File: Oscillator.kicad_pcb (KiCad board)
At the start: 2 copper layers, 200.9 x 113.3 mm, 231 parts, among them J201 AudioJack2, J202 AudioJack2, J203 AudioJack2, J204 Conn_01x14, J205 AudioJack2, J206 AudioJack2, J207 Conn_01x09, J208 AudioJack2, J209 AudioJack2, J210 AudioJack2, J301 Conn_01x14, J302 Conn_01x09, J303 Conn_02x05_Odd_Even, Q401 2N3904, Q402 2N3906, Q403 2N3904, Q601 Q_NJFET_DSG, Q602 Q_NJFET_DSG, Q603 2N3904, Q701 Q_NJFET_DSG, SW201 SR1712F-0204-20F0A-N9-N-027, U201 TL072, U402 LM13700, U501 TL074, U502 LM13700, U503 TL074, U601 TL074, U602 LM339, U603 TL074, U604 4066, U605 TL074, U701 OP275, U702 DMMT3904W, U703 TL072

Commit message: Added version markings
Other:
- board text added: "oscillator / waveshaper / vca version 2 chris defrancisci"
- board text removed: "oscillator / waveshaper / vca version 1 chris defrancisci"

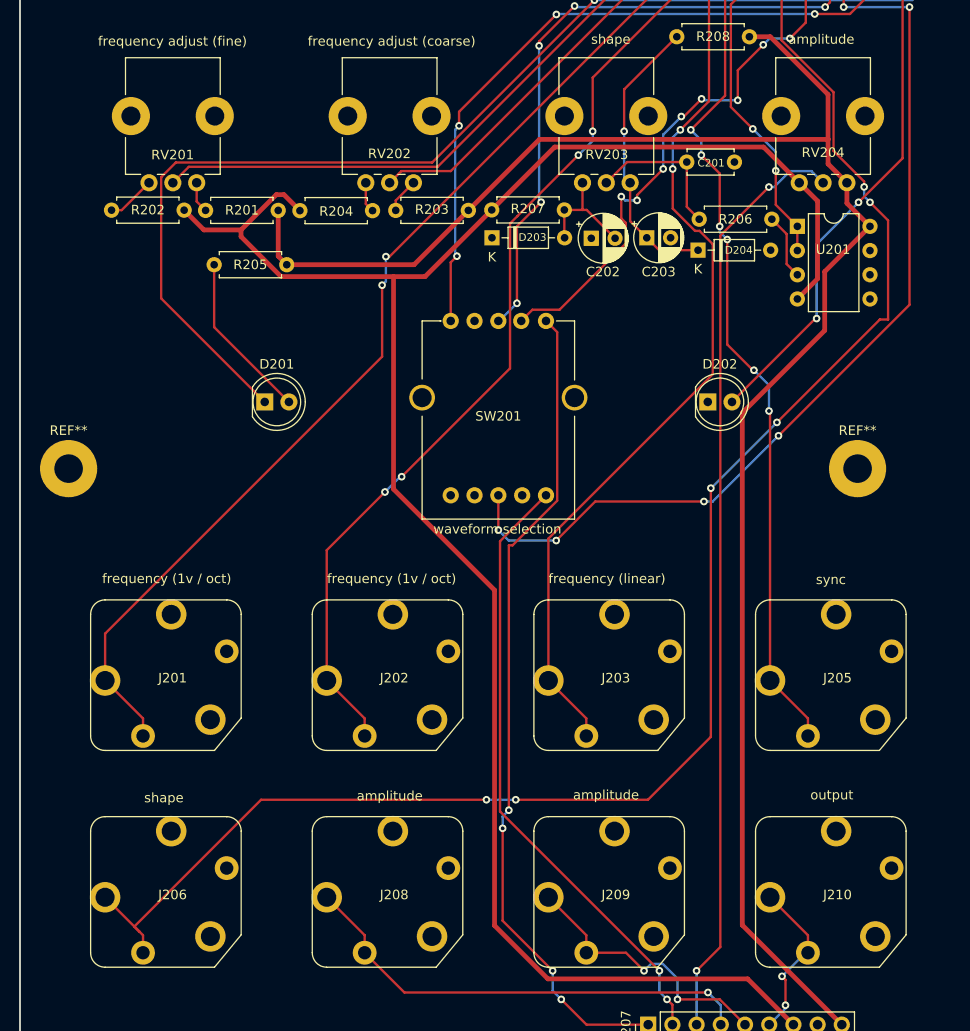
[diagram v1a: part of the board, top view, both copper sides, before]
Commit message: Updated for tayda pots A-5513 and jacks A-2563
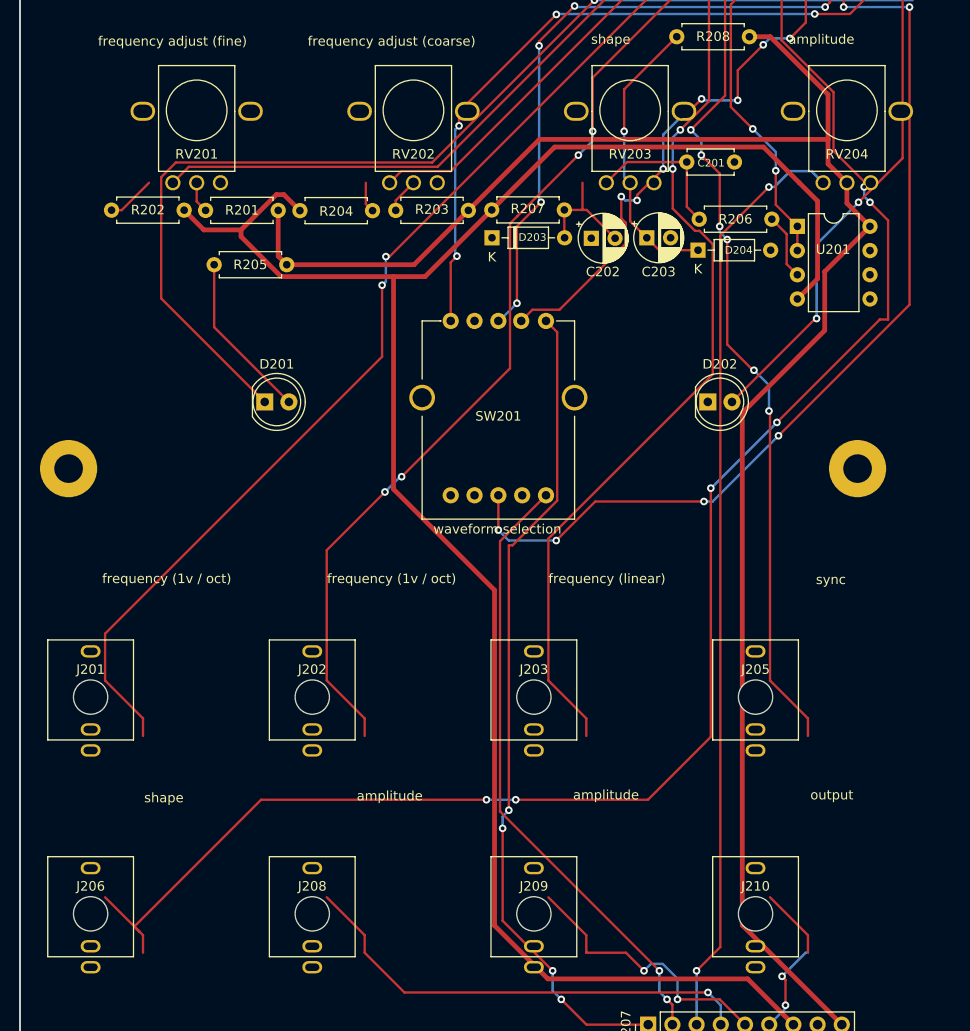
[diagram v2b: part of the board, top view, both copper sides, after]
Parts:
- J201, J202, J203, J205, J206, J208, J209, J210: footprint ACJM-MV35:ACJM-MV35 -> A-2563:A-2563
- RV201, RV202, RV203, RV204: footprint Potentiometer_THT:Potentiometer_Bourns_PTV09A-1_Single_Vertical -> A-5513:A-5513
- turned RV201 to 0 degrees
- turned RV202 to 0 degrees
- turned RV203 to 0 degrees
- turned RV204 to 0 degrees
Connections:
- RV201 pad 1: Net-(R201-Pad2) -> Net-(R202-Pad1)
- RV201 pad 3: Net-(R202-Pad1) -> Net-(R201-Pad2)
- RV202 pad 1: Net-(R203-Pad2) -> Net-(R204-Pad1)
- RV202 pad 3: Net-(R204-Pad1) -> Net-(R203-Pad2)
- RV203 pad 1: Net-(C203-Pad1) -> Net-(C202-Pad2)
- RV203 pad 3: Net-(C202-Pad2) -> Net-(C203-Pad1)
- RV204 pad 1: +12V -> -12V
- RV204 pad 3: -12V -> +12V

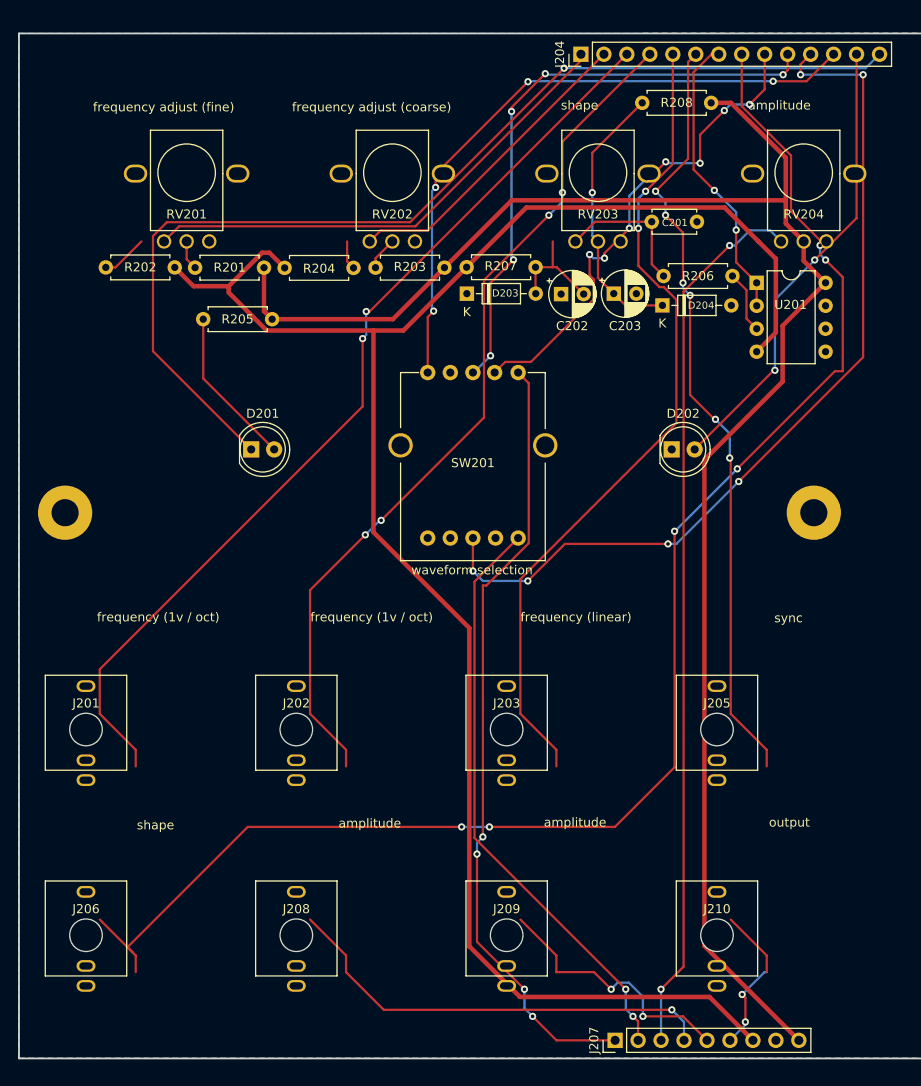
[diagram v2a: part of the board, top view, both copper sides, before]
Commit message: Arranging/connecting new knobs/jacks
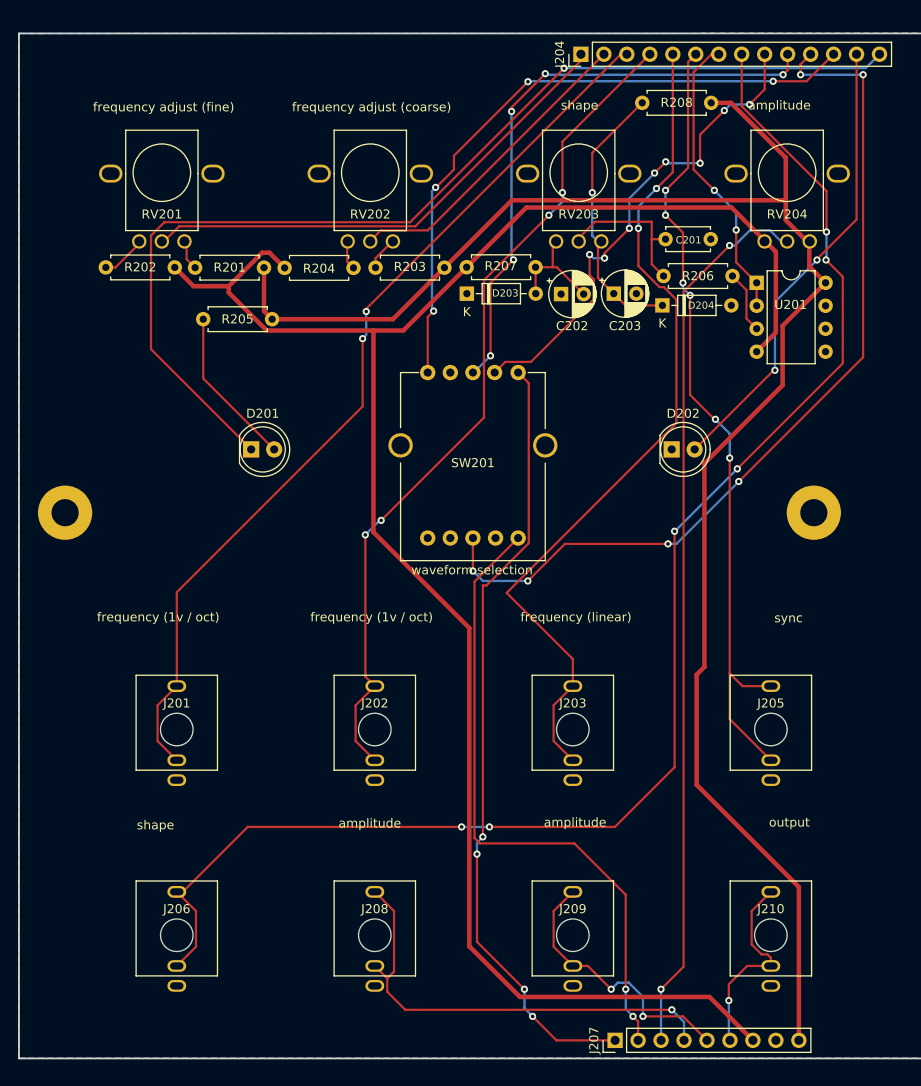
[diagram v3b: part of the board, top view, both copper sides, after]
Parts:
- moved J201 10.0 mm to (84.5, 112.6)
- moved J206 10.0 mm to (84.5, 135.3)
- moved J202 8.68 mm to (106.4, 112.6)
- moved J208 8.68 mm to (106.4, 135.3)
- moved J203 7.32 mm to (128.3, 112.6)
- moved J209 7.32 mm to (128.3, 135.3)
- moved J205 5.96 mm to (150.2, 112.6)
- moved J210 5.96 mm to (150.2, 135.3)
- moved RV201 2.74 mm to (82.8, 53.0)
- moved C201 2.46 mm to (138.6, 52.8)
- moved RV202 2.44 mm to (105.9, 53.0)
- moved RV203 2.13 mm to (128.9, 53.0)
- moved RV204 1.83 mm to (152.0, 53.0)
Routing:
- net /panel/shape_cv: track 168.7 -> 162.0 mm
- net /panel/waveshaper_bypass: track 65.0 -> 71.2 mm
- net /panel/out: track 17.1 -> 22.1 mm, vias 2 -> 1
- net /panel/fm_cv1: track 104.8 -> 100.8 mm
- net /panel/sync: track 85.7 -> 89.6 mm
- net /panel/fm_cv_lin: track 91.1 -> 94.2 mm
- net /panel/fm_cv2: track 96.1 -> 93.4 mm
- net Net-(C201-Pad1): track 15.9 -> 17.4 mm
- net /panel/vca_cv1: track 49.2 -> 50.4 mm
- net /panel/vca_cv2: track 29.1 -> 30.1 mm
- net +12V: track 687.9 -> 688.6 mm

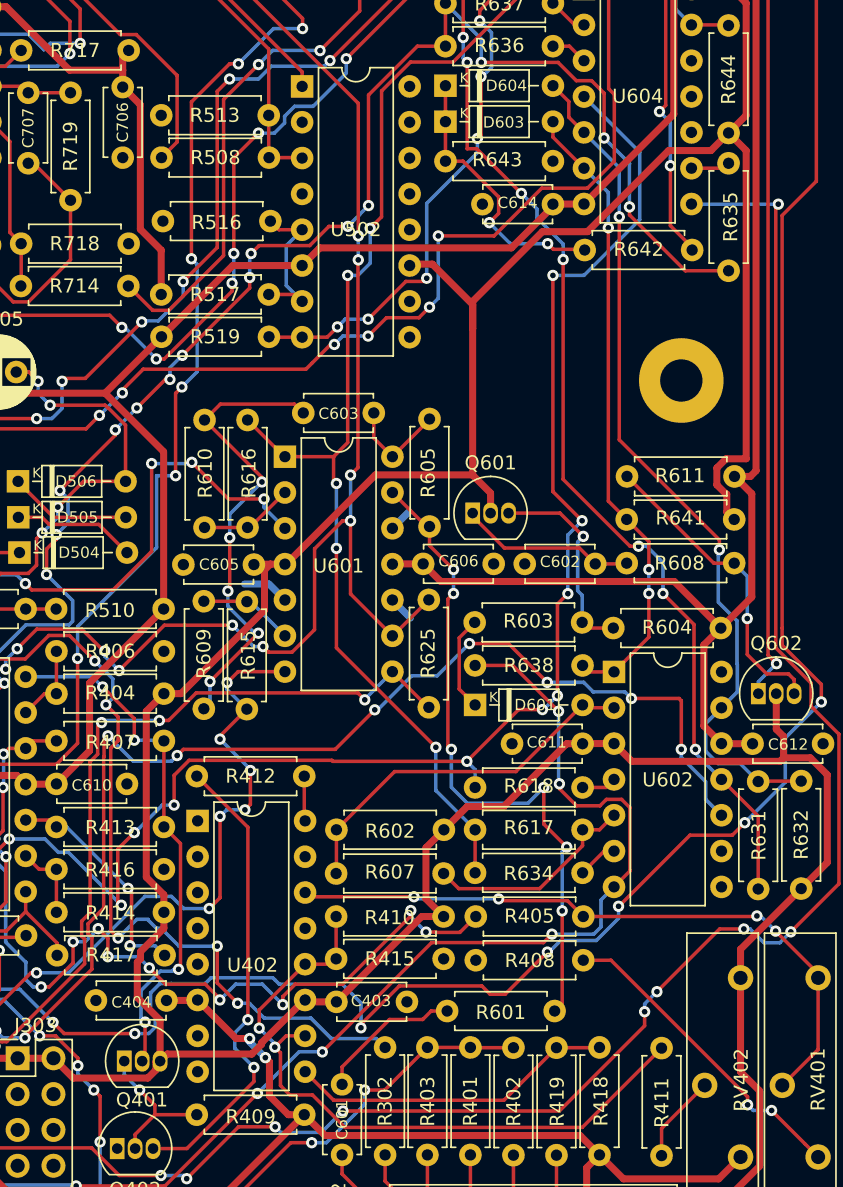
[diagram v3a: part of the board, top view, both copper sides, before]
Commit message: Routed consolidate lm13700, ran DRC
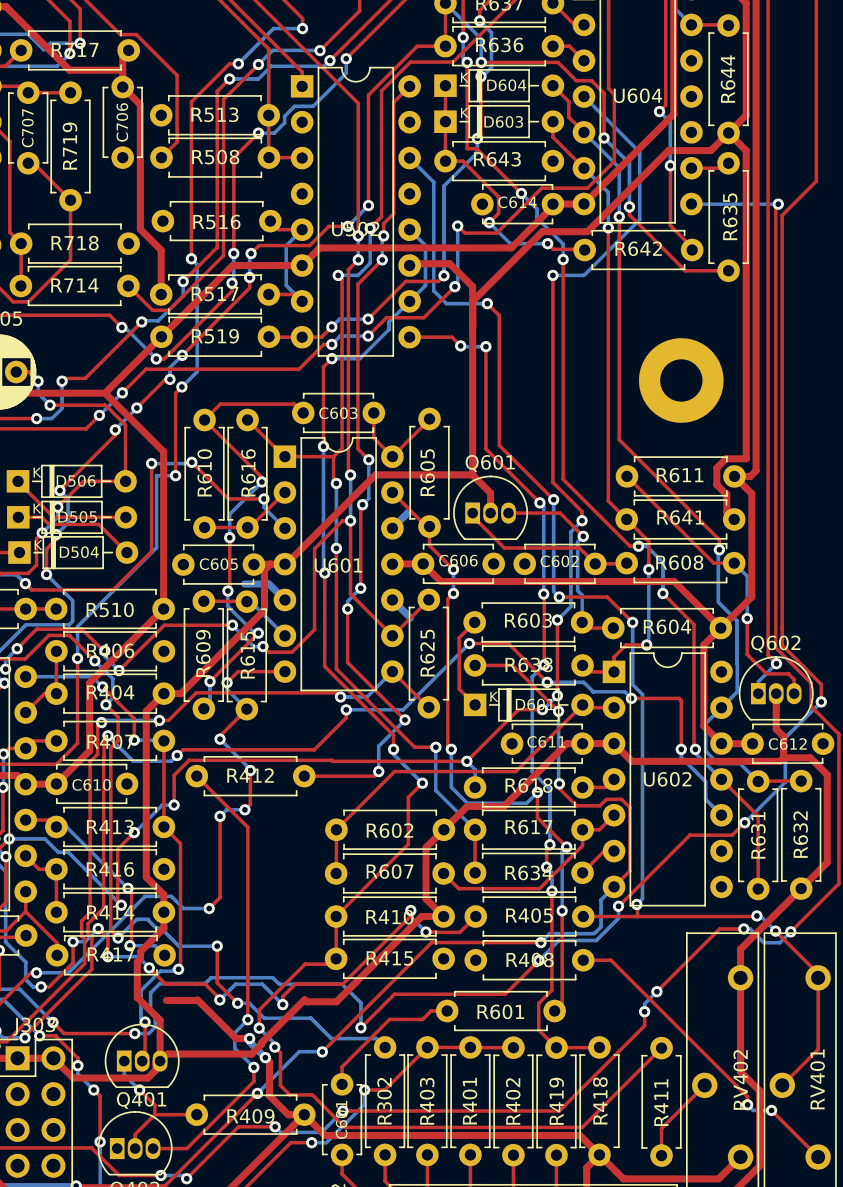
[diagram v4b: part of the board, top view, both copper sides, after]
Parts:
- removed C403, C404: .1u, Capacitor_THT:C_Disc_D4.7mm_W2.5mm_P5.00mm
- removed U402: LM13700, Package_DIP:DIP-16_W7.62mm
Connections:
- U502 pad 10: (no net) -> Net-(R410-Pad1)
- U502 pad 12: (no net) -> Net-(R410-Pad1)
- U502 pad 13: (no net) -> GND
- U502 pad 14: (no net) -> Net-(R405-Pad1)
- U502 pad 16: (no net) -> Net-(R412-Pad2)
- U502 pad 9: (no net) -> Net-(R418-Pad1)
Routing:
- net Net-(R410-Pad1): track 49.0 -> 105.3 mm, vias 2 -> 7
- net Net-(R412-Pad2): track 3.19 -> 58.9 mm, vias 0 -> 8
- net Net-(R405-Pad1): track 47.8 -> 91.8 mm, vias 4 -> 7
- net Net-(R418-Pad1): track 23.3 -> 62.2 mm, vias 0 -> 8
- net /main/WAVESHAPER/Mid_bias_signal: track 87.6 -> 89.1 mm
- net Net-(D603-Pad2): track 45.3 -> 46.1 mm
- net Net-(R601-Pad1): track 47.5 -> 46.7 mm
- net +12V: track 688.6 -> 689.4 mm
- net /main/VCA/LED: track 157.7 -> 157.1 mm
- net Net-(R518-Pad2): track 58.5 -> 59.1 mm

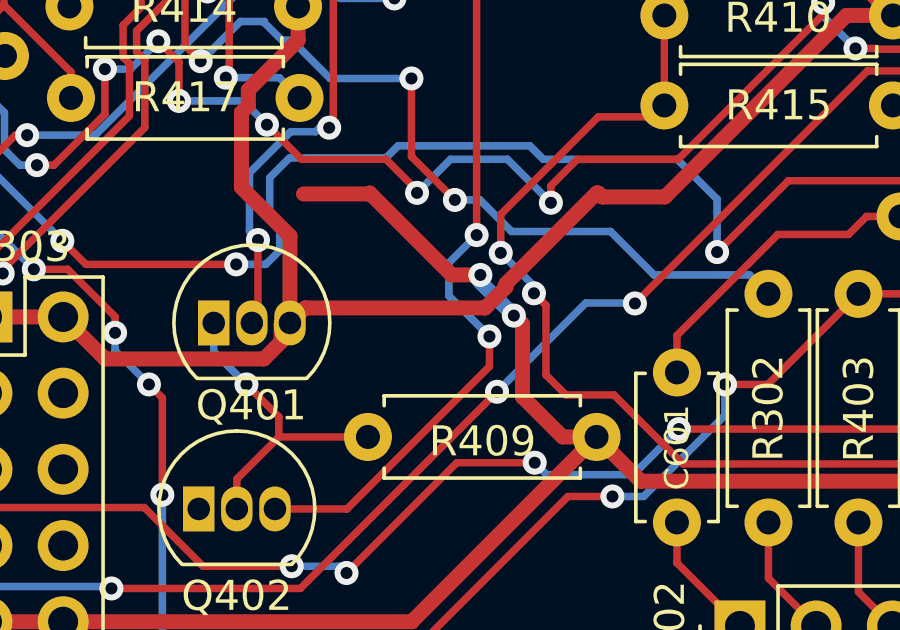
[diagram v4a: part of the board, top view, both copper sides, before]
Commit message: Removed extra trace, ran DRC
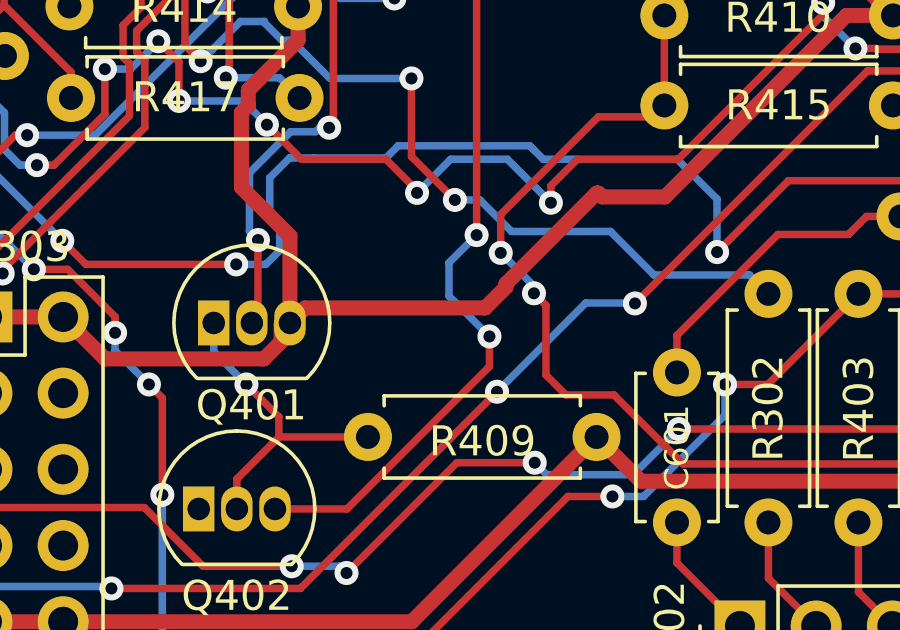
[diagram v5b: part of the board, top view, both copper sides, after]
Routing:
- net -12V: track 651.5 -> 636.8 mm, vias 2 -> 0
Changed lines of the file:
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@@
     (thickness 1.6)
     (drawings 53)
-    (tracks 2989)
+    (tracks 2977)
     (zones 0)
     (modules 228)
@@
   (segment (start 238.350001 97.250001) (end 254.900001 97.250001) (width 0.5) (layer F.Cu) (net 6))
   (segment (start 237.1 96) (end 238.350001 97.250001) (width 0.5) (layer F.Cu) (net 6))
-  (segment (start 221.08 126.95) (end 221.11 126.92) (width 0.5) (layer F.Cu) (net 6))
-  (segment (start 218.9 126.95) (end 221.08 126.95) (width 0.5) (layer F.Cu) (net 6))
   (segment (start 190.02 91.52) (end 191.5 93) (width 0.5) (layer F.Cu) (net 6))
   (segment (start 189.32 91.52) (end 190.02 91.52) (width 0.5) (layer F.Cu) (net 6))
@@
   (segment (start 248.225011 136.525011) (end 230.145011 136.525011) (width 0.5) (layer F.Cu) (net 6))
   (segment (start 249.6 137.9) (end 248.225011 136.525011) (width 0.5) (layer F.Cu) (net 6))
-  (segment (start 226.202184 133.713554) (end 226.202184 131.292911) (width 0.5) (layer F.Cu) (net 6))
-  (segment (start 221.11 126.92) (end 223.839593 129.649593) (width 0.5) (layer F.Cu) (net 6))
-  (via (at 224.798381 129.649593) (size 0.8) (drill 0.4) (layers F.Cu B.Cu) (net 6))
-  (segment (start 223.839593 129.649593) (end 224.798381 129.649593) (width 0.5) (layer F.Cu) (net 6))
-  (segment (start 228.67 135.05) (end 227.53863 135.05) (width 0.5) (layer F.Cu) (net 6))
-  (segment (start 226.202184 131.292911) (end 225.91379 131.004517) (width 0.5) (layer F.Cu) (net 6))
-  (segment (start 224.798381 129.889108) (end 225.91379 131.004517) (width 0.5) (layer B.Cu) (net 6))
-  (segment (start 227.53863 135.05) (end 226.202184 133.713554) (width 0.5) (layer F.Cu) (net 6))
-  (via (at 225.91379 131.004517) (size 0.8) (drill 0.4) (layers F.Cu B.Cu) (net 6))
-  (segment (start 224.798381 129.649593) (end 224.798381 129.889108) (width 0.5) (layer B.Cu) (net 6))
   (segment (start 186 39.738002) (end 186 35.2) (width 0.5) (layer F.Cu) (net 6))
   (segment (start 188.250001 61.750001) (end 188.250001 41.988003) (width 0.5) (layer F.Cu) (net 6))
